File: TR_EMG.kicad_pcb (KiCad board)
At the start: 4 copper layers, 118.1 x 101.6 mm, 118 parts, among them J1 1727230, J2 1727230, J3 1844236, J4 MJ-3523-SMT-TR, J5 MJ-3523-SMT-TR, J6 MJ-3523-SMT-TR, J7 MJ-3523-SMT-TR, U1 ADS1115IDGSR, U101 INA115BU, U111 LT1169CS8-PBF, U112 LT1169CS8-PBF, U201 INA115BU, U211 LT1169CS8-PBF, U212 LT1169CS8-PBF, U301 INA115BU, U311 LT1169CS8-PBF, U312 LT1169CS8-PBF, U401 INA115BU, U411 LT1169CS8-PBF, U412 LT1169CS8-PBF

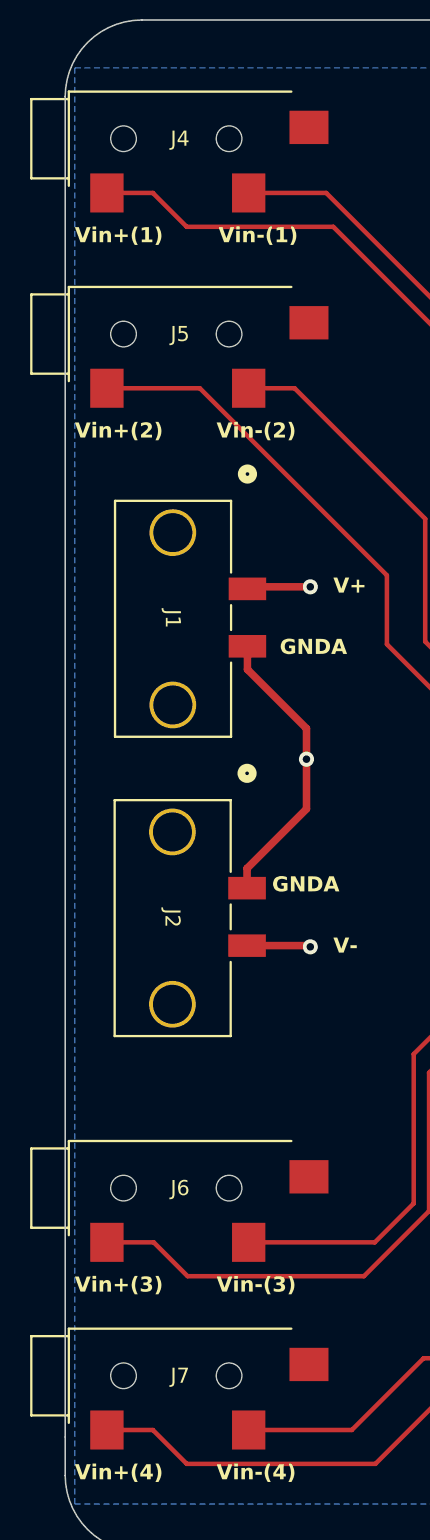
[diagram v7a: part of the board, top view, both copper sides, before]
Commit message: nore footprint tweaking to meet DRC requirements
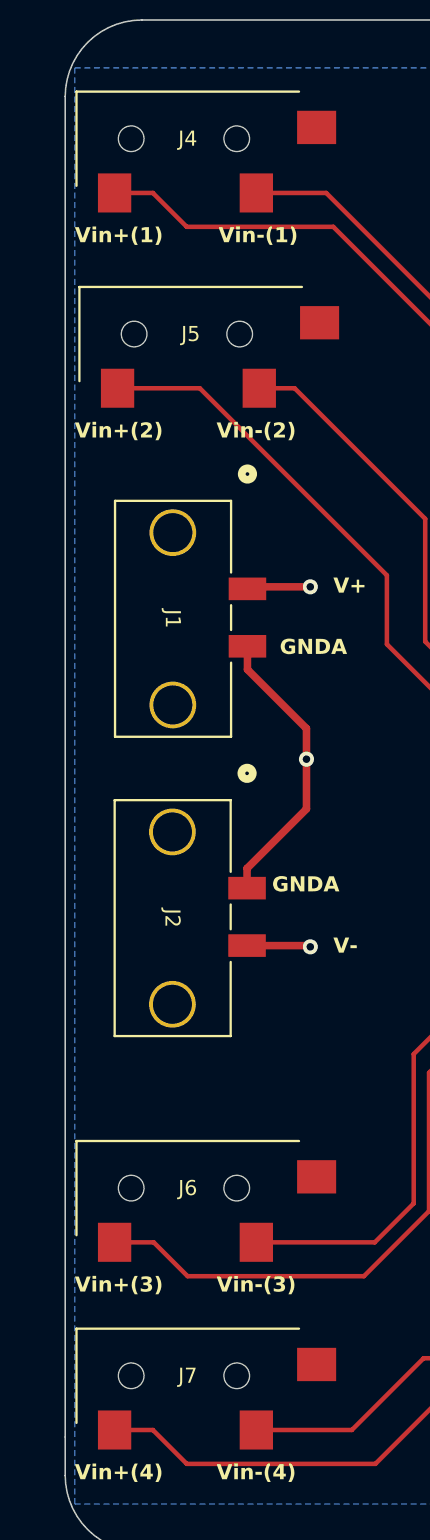
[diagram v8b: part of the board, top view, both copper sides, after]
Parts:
- moved J5 0.70 mm to (97.2, 58.9)
- moved J4 0.51 mm to (97.0, 46.0)
- moved J6 0.51 mm to (97.0, 115.6)
- moved J7 0.51 mm to (97.0, 128.0)
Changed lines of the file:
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@@
   )
   (footprint "footprints:CONN_MJ-3523_CUD_CtYrd" (layer "F.Cu")
-    (at 96.52 45.974)
+    (at 97.028 45.974)
     (tags "MJ-3523-SMT-TR ")
     (property "LCSC" "")
@@
         (effects (font (size 1 1) (thickness 0.15)))
     )
-    (fp_line (start -9.8679 -2.6289) (end -9.8679 2.6289)
-      (stroke (width 0.1524) (type solid)) (layer "F.SilkS"))
-    (fp_line (start -9.8679 2.6289) (end -7.3787 2.6289)
-      (stroke (width 0.1524) (type solid)) (layer "F.SilkS"))
     (fp_line (start -7.3787 -3.1242) (end -7.3787 3.1242)
       (stroke (width 0.1524) (type solid)) (layer "F.SilkS"))
-    (fp_line (start -7.3787 -2.6289) (end -9.8679 -2.6289)
-      (stroke (width 0.1524) (type solid)) (layer "F.SilkS"))
     (fp_line (start 7.3787 -3.1242) (end -7.3787 -3.1242)
       (stroke (width 0.1524) (type solid)) (layer "F.SilkS"))
@@
   )
   (footprint "footprints:CONN_MJ-3523_CUD_CtYrd" (layer "F.Cu")
-    (at 96.52 128.016)
+    (at 97.028 128.016)
     (tags "MJ-3523-SMT-TR ")
     (property "LCSC" "")
@@
         (effects (font (size 1 1) (thickness 0.15)))
     )
-    (fp_line (start -9.8679 -2.6289) (end -9.8679 2.6289)
-      (stroke (width 0.1524) (type solid)) (layer "F.SilkS"))
-    (fp_line (start -9.8679 2.6289) (end -7.3787 2.6289)
-      (stroke (width 0.1524) (type solid)) (layer "F.SilkS"))
     (fp_line (start -7.3787 -3.1242) (end -7.3787 3.1242)
       (stroke (width 0.1524) (type solid)) (layer "F.SilkS"))
-    (fp_line (start -7.3787 -2.6289) (end -9.8679 -2.6289)
-      (stroke (width 0.1524) (type solid)) (layer "F.SilkS"))
     (fp_line (start 7.3787 -3.1242) (end -7.3787 -3.1242)
       (stroke (width 0.1524) (type solid)) (layer "F.SilkS"))
@@
   )
   (footprint "footprints:CONN_MJ-3523_CUD_CtYrd" (layer "F.Cu")
-    (at 96.52 58.928)
+    (at 97.2237 58.928)
     (tags "MJ-3523-SMT-TR ")
     (property "LCSC" "")
@@
         (effects (font (size 1 1) (thickness 0.15)))
     )
-    (fp_line (start -9.8679 -2.6289) (end -9.8679 2.6289)
-      (stroke (width 0.1524) (type solid)) (layer "F.SilkS"))
-    (fp_line (start -9.8679 2.6289) (end -7.3787 2.6289)
-      (stroke (width 0.1524) (type solid)) (layer "F.SilkS"))
     (fp_line (start -7.3787 -3.1242) (end -7.3787 3.1242)
       (stroke (width 0.1524) (type solid)) (layer "F.SilkS"))
-    (fp_line (start -7.3787 -2.6289) (end -9.8679 -2.6289)
-      (stroke (width 0.1524) (type solid)) (layer "F.SilkS"))
     (fp_line (start 7.3787 -3.1242) (end -7.3787 -3.1242)
       (stroke (width 0.1524) (type solid)) (layer "F.SilkS"))
@@
   )
   (footprint "footprints:CONN_MJ-3523_CUD_CtYrd" (layer "F.Cu")
-    (at 96.52 115.57)
+    (at 97.028 115.57)
     (tags "MJ-3523-SMT-TR ")
     (property "LCSC" "")
@@
         (effects (font (size 1 1) (thickness 0.15)))
     )
-    (fp_line (start -9.8679 -2.6289) (end -9.8679 2.6289)
-      (stroke (width 0.1524) (type solid)) (layer "F.SilkS"))
-    (fp_line (start -9.8679 2.6289) (end -7.3787 2.6289)
-      (stroke (width 0.1524) (type solid)) (layer "F.SilkS"))
     (fp_line (start -7.3787 -3.1242) (end -7.3787 3.1242)
       (stroke (width 0.1524) (type solid)) (layer "F.SilkS"))
-    (fp_line (start -7.3787 -2.6289) (end -9.8679 -2.6289)
-      (stroke (width 0.1524) (type solid)) (layer "F.SilkS"))
     (fp_line (start 7.3787 -3.1242) (end -7.3787 -3.1242)
